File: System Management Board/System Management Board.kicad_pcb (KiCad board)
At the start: 4 copper layers, 150 x 110 mm, 55 parts, among them J1 Conn_01x04_Male, J2 Conn_01x04_Male, J3 Conn_01x02_Male, J4 PJ-063BH, J5 Conn_01x02_Male, J6 Conn_02x06_Counter_Clockwise, J7 Conn_02x20_Odd_Even, J8 Conn_01x02_Male, J9 Conn_01x02_Male, K1 J115F11CH5VDCS61.5U, K2 J114FL1CS165VDC.41, K3 J114FL1CS165VDC.41, U1 SC0915, U2 OKI-78SR-5/1.5-W36E-C, U3 OKI-78SR-5/1.5-W36E-C, U4 NEO-M9N-00B

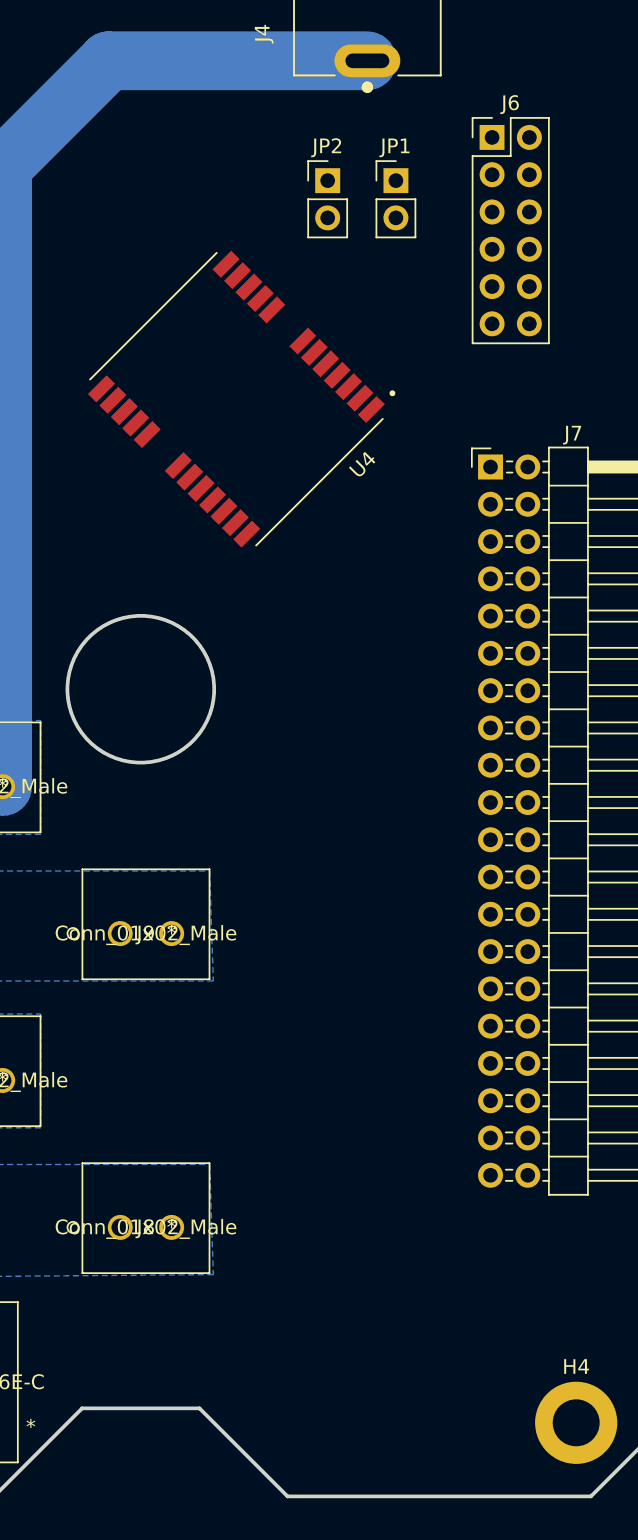
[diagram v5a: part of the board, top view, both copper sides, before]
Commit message: Removed GPS module, added GPIO connections to headder, added aux jetson header
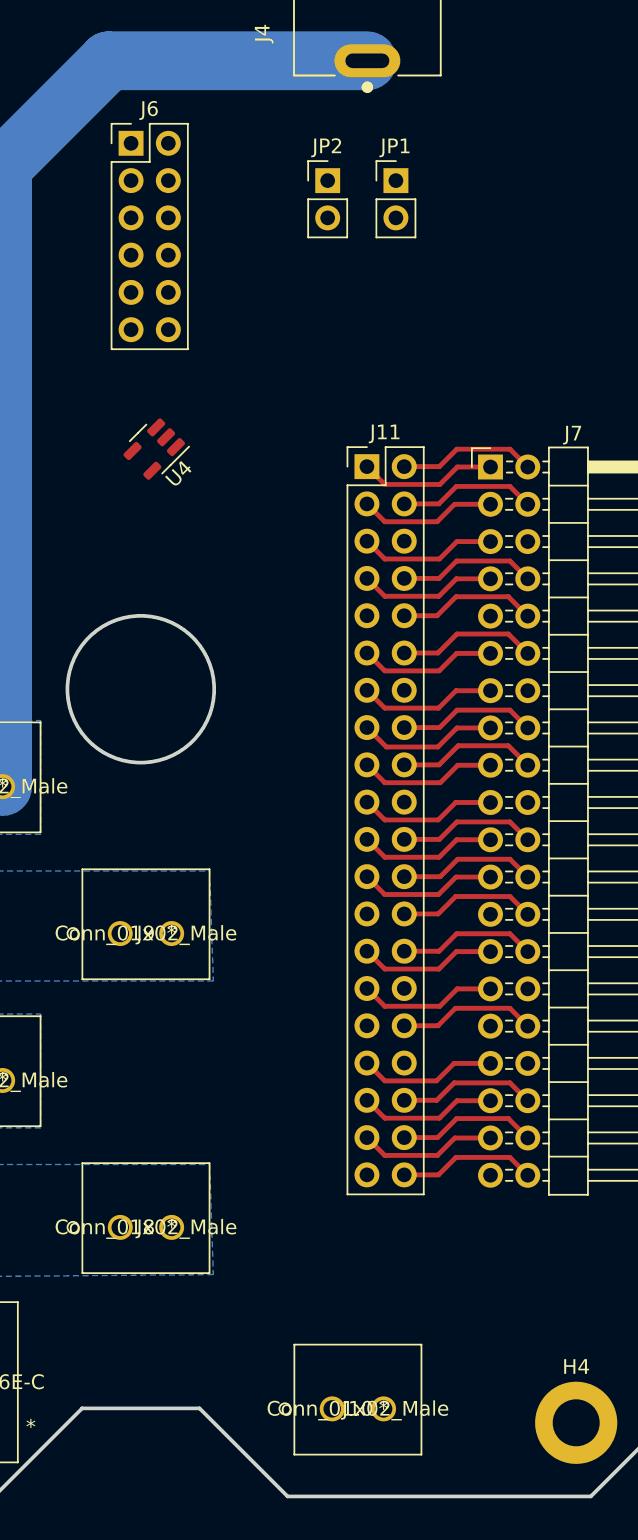
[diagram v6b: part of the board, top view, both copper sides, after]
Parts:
- added J10: Conn_01x02_Male, SMB:1843606, F.Cu at (203.6, 149.4)
- added J11: Conn_02x20_Odd_Even, Connector_PinHeader_2.54mm:PinHeader_2x20_P2.54mm_Vertical, F.Cu at (202.5, 85.2)
- U4: value NEO-M9N-00B -> AP7375-50W5-7; footprint SMB:XCVR_NEO-M9N-00B -> Package_TO_SOT_SMD:SOT-23-5
- moved J6 24.6 mm to (186.4, 63.2)
- moved U4 6.55 mm to (188.0, 84.0)
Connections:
- J7 pad 1: unconnected-(J7-Pad1) -> /JET_P1
- J7 pad 10: unconnected-(J7-Pad10) -> /Jet_UART1_Rx
- J7 pad 11: unconnected-(J7-Pad11) -> /JET_P11
- J7 pad 12: unconnected-(J7-Pad12) -> /JET_P12
- J7 pad 13: unconnected-(J7-Pad13) -> /PICO OUT BIT 1
- J7 pad 14: unconnected-(J7-Pad14) -> GND
- J7 pad 15: unconnected-(J7-Pad15) -> /PICO OUT BIT 0
- J7 pad 16: unconnected-(J7-Pad16) -> /PICO IN BIT 0
- J7 pad 17: unconnected-(J7-Pad17) -> /JET_P17
- J7 pad 18: unconnected-(J7-Pad18) -> /PICO OUT BIT 2
- J7 pad 19: unconnected-(J7-Pad19) -> /JET_P19
- J7 pad 2: unconnected-(J7-Pad2) -> /JET_P2
- J7 pad 20: unconnected-(J7-Pad20) -> GND
- J7 pad 21: unconnected-(J7-Pad21) -> /JET_P21
- J7 pad 22: unconnected-(J7-Pad22) -> /PICO IN BIT 2
- J7 pad 23: unconnected-(J7-Pad23) -> /JET_P23
- J7 pad 24: unconnected-(J7-Pad24) -> /JET_P24
- J7 pad 25: unconnected-(J7-Pad25) -> GND
- J7 pad 26: unconnected-(J7-Pad26) -> /JET_P26
- J7 pad 27: unconnected-(J7-Pad27) -> /JET_P27
- J7 pad 28: unconnected-(J7-Pad28) -> /JET_P28
- J7 pad 29: unconnected-(J7-Pad29) -> /JET_P29
- J7 pad 3: unconnected-(J7-Pad3) -> /JET_P3
- J7 pad 30: unconnected-(J7-Pad30) -> GND
- J7 pad 31: unconnected-(J7-Pad31) -> /JET_P31
- J7 pad 32: unconnected-(J7-Pad32) -> /PICO IN BIT 1
- J7 pad 33: unconnected-(J7-Pad33) -> /JET_P33
- J7 pad 34: unconnected-(J7-Pad34) -> GND
- J7 pad 35: unconnected-(J7-Pad35) -> /JET_P35
- J7 pad 36: unconnected-(J7-Pad36) -> /JET_P36
- J7 pad 37: unconnected-(J7-Pad37) -> /JET_P37
- J7 pad 38: unconnected-(J7-Pad38) -> /JET_P38
- J7 pad 39: unconnected-(J7-Pad39) -> GND
- J7 pad 4: unconnected-(J7-Pad4) -> /JET_P4
- J7 pad 40: unconnected-(J7-Pad40) -> /JET_P40
- J7 pad 5: unconnected-(J7-Pad5) -> /JET_P5
- J7 pad 6: unconnected-(J7-Pad6) -> GND
- J7 pad 7: unconnected-(J7-Pad7) -> /JET_P7
- J7 pad 8: unconnected-(J7-Pad8) -> /Jet_UART1_Tx
- J7 pad 9: unconnected-(J7-Pad9) -> GND
- U1 pad 1: unconnected-(U1-Pad1) -> /PICO IN BIT 0
- U1 pad 2: unconnected-(U1-Pad2) -> /PICO IN BIT 1
- U1 pad 31: unconnected-(U1-Pad31) -> /Vin_MES_ADC
- U1 pad 39: unconnected-(U1-Pad39) -> /5V Logic PWR
- U1 pad 4: unconnected-(U1-Pad4) -> /PICO IN BIT 2
- U1 pad 5: unconnected-(U1-Pad5) -> /PICO OUT BIT 0
- U1 pad 6: unconnected-(U1-Pad6) -> /PICO OUT BIT 1
- U1 pad 7: unconnected-(U1-Pad7) -> /PICO OUT BIT 2
- U2 pad 1: unconnected-(U2-Pad1) -> /V_batt+ PROT SW
- U2 pad 2: unconnected-(U2-Pad2) -> GND
- U2 pad 3: unconnected-(U2-Pad3) -> /5V Relay PWR
- U3 pad 1: unconnected-(U3-Pad1) -> /V_batt+ PROT SW
- U3 pad 2: unconnected-(U3-Pad2) -> GND
- U3 pad 3: unconnected-(U3-Pad3) -> /5V Logic PWR
- U4 pad 1: unconnected-(U4-Pad1) -> /V_batt+ PROT
- U4 pad 2: unconnected-(U4-Pad2) -> GND
- U4 pad 3: unconnected-(U4-Pad3) -> /Switched PWR IN PROT
- U4 pad 4: unconnected-(U4-Pad4) -> (no net)
- U4 pad 5: unconnected-(U4-Pad5) -> /5V Logic PWR
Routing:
- net /JET_P38: track 0.00 -> 9.51 mm
- net /PICO OUT BIT 2: track 0.00 -> 9.51 mm
- net /Jet_UART1_Rx: track 0.00 -> 9.51 mm
- net /PICO OUT BIT 0: track 0.00 -> 9.51 mm
- net /JET_P12: track 0.00 -> 9.50 mm
- net /PICO IN BIT 0: track 0.00 -> 9.41 mm
- net /Jet_UART1_Tx: track 0.00 -> 9.41 mm
- net /JET_P36: track 0.00 -> 9.41 mm
- net /JET_P26: track 0.00 -> 9.41 mm
- net /JET_P40: track 0.00 -> 9.41 mm
- net /JET_P2: track 0.00 -> 9.41 mm
- net /JET_P7: track 0.00 -> 9.41 mm
- net /JET_P5: track 0.00 -> 9.41 mm
- net /JET_P37: track 0.00 -> 9.41 mm
- net /JET_P35: track 0.00 -> 9.41 mm
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
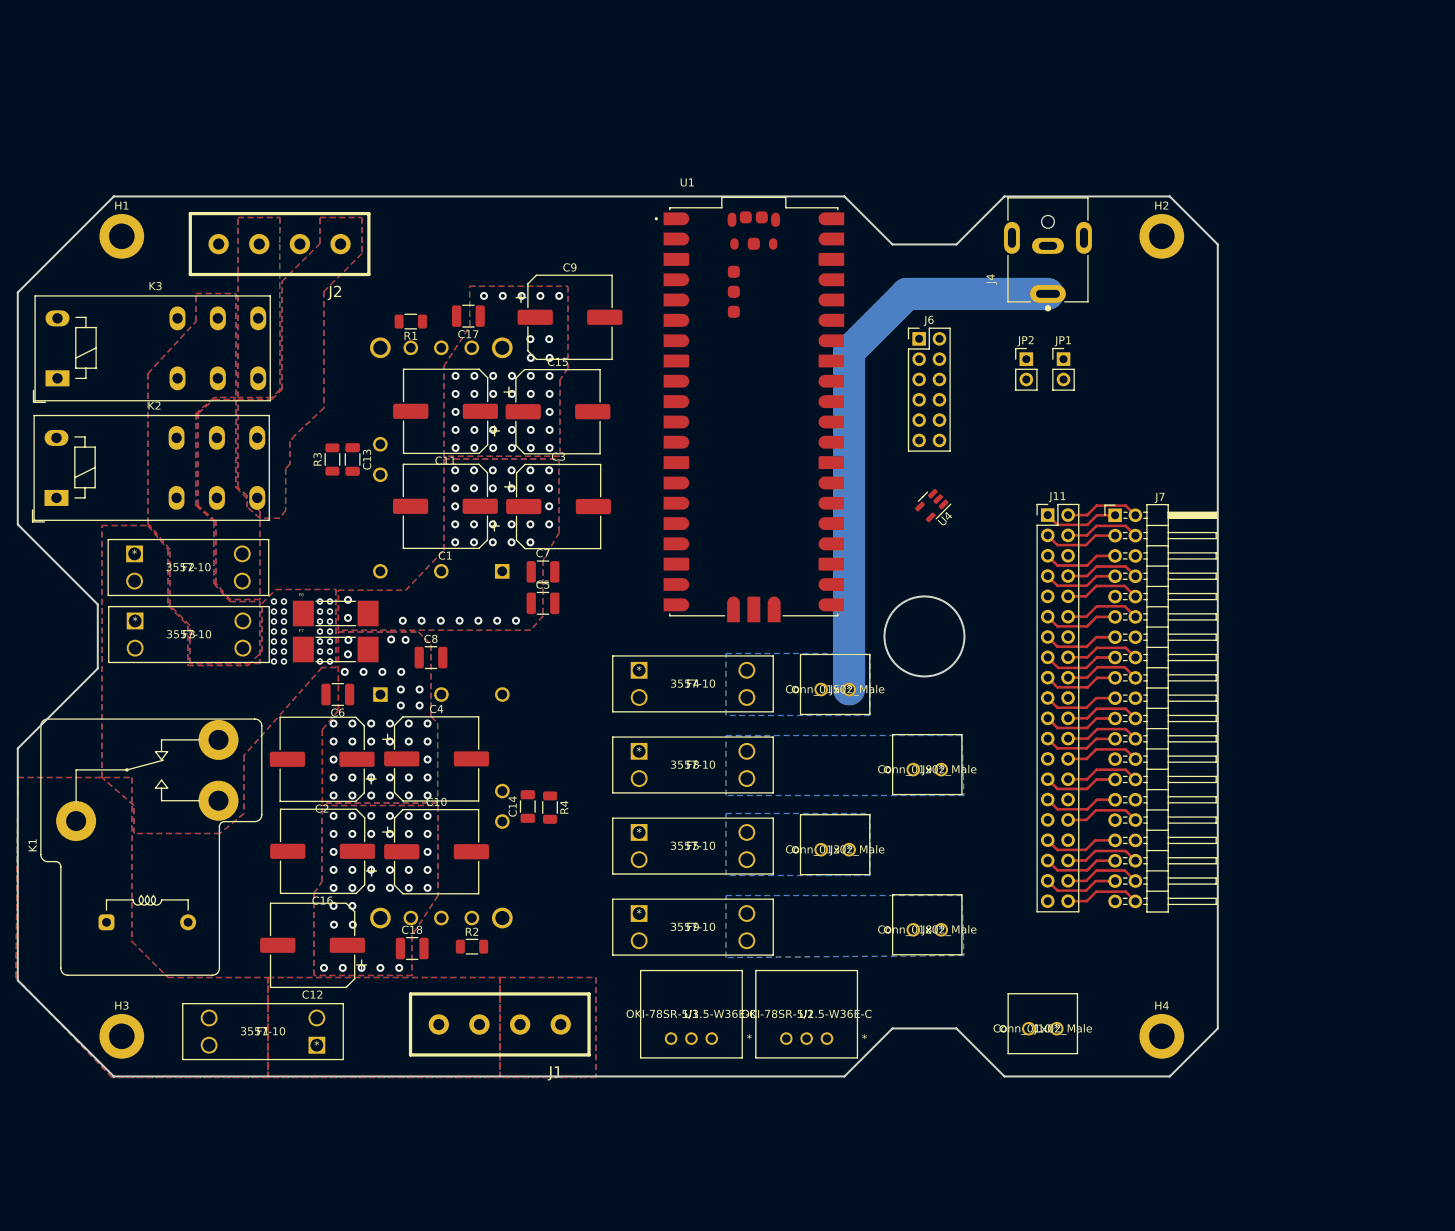
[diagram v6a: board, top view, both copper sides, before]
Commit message: Finished all high current connections
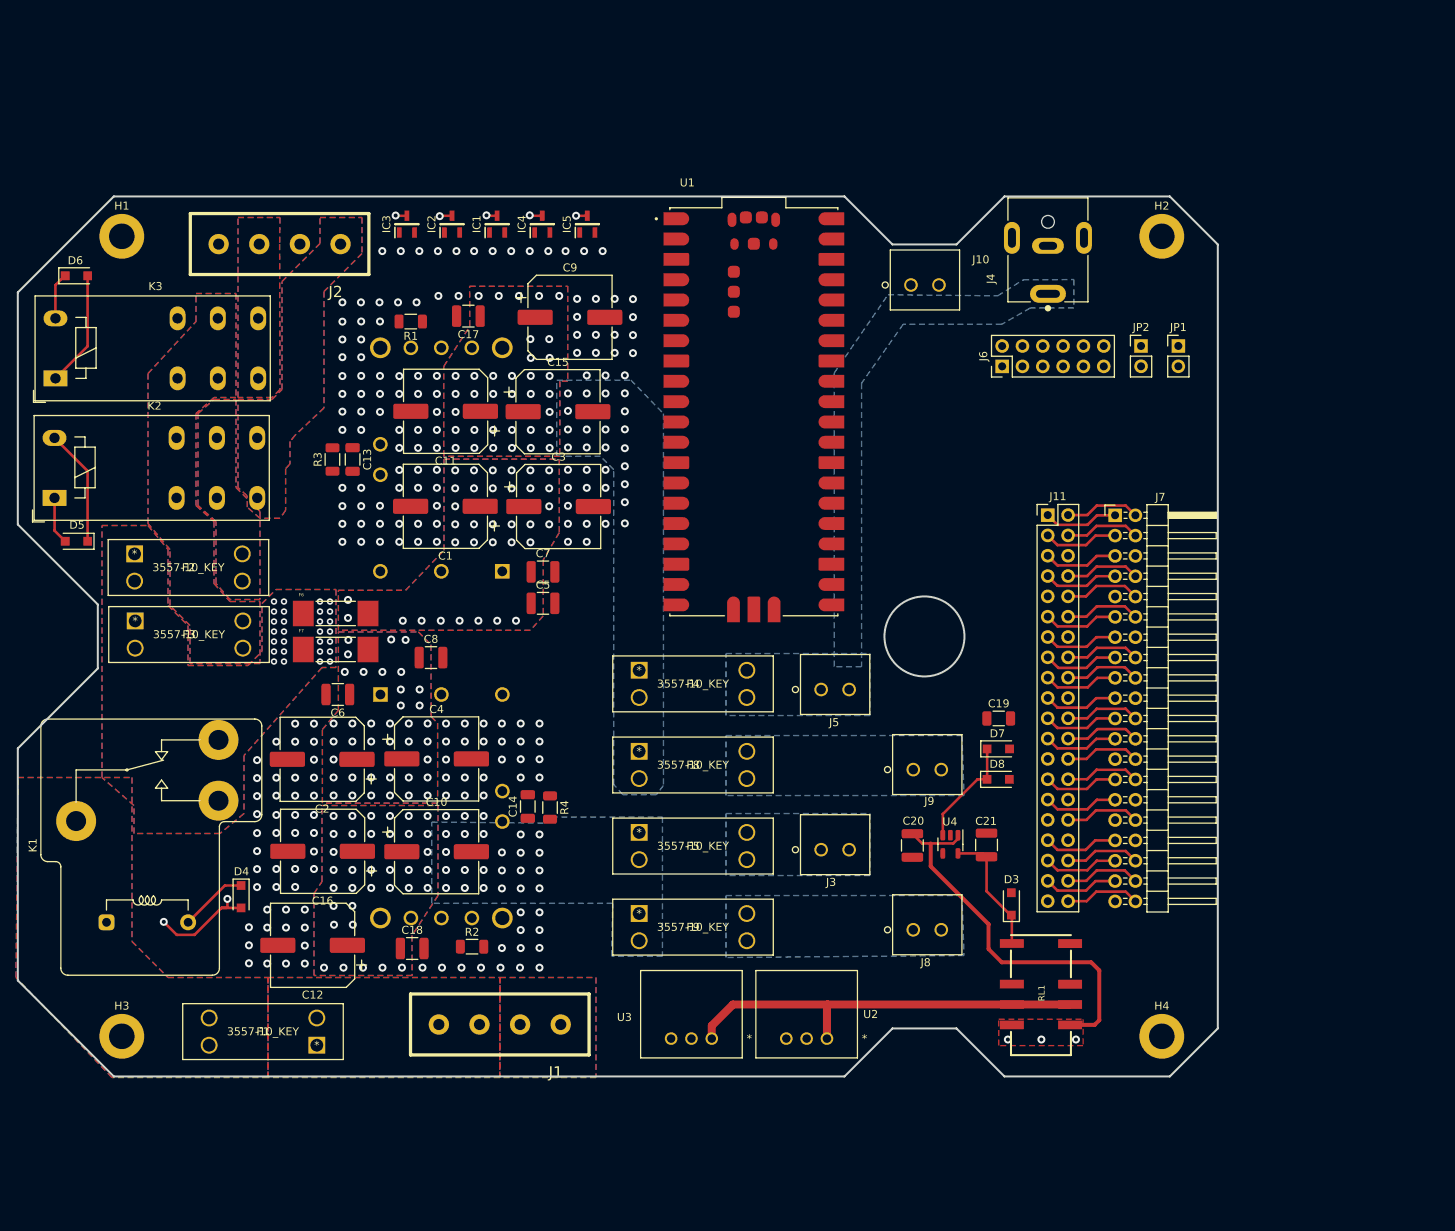
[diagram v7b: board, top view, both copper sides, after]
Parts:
- added C19: 0.1uF, Capacitor_SMD:C_1206_3216Metric, F.Cu at (196.3, 110.6)
- added C20: 10uF, Capacitor_SMD:C_1210_3225Metric, F.Cu at (185.5, 126.5)
- added C21: 10uF, Capacitor_SMD:C_1210_3225Metric, F.Cu at (194.8, 126.4)
- added D3: D, Diode_SMD:D_SOD-123F, F.Cu at (197.9, 133.8)
- added D4: D, Diode_SMD:D_SOD-123F, F.Cu at (101.6, 132.9)
- added D5: D, Diode_SMD:D_SOD-123F, F.Cu at (81.1, 88.5)
- added D6: D, Diode_SMD:D_SOD-123F, F.Cu at (81.1, 55.3)
- added D7: D, Diode_SMD:D_SOD-123F, F.Cu at (196.3, 114.4)
- added D8: D, Diode_SMD:D_SOD-123F, F.Cu at (196.3, 118.2)
- added IC1: SI2318CDS-T1-GE3, SMB:SOT95P237X112-3N, F.Cu at (133.6, 48.8)
- added IC2: SI2318CDS-T1-GE3, SMB:SOT95P237X112-3N, F.Cu at (128.0, 48.8)
- added IC3: SI2318CDS-T1-GE3, SMB:SOT95P237X112-3N, F.Cu at (122.4, 48.8)
- added IC4: SI2318CDS-T1-GE3, SMB:SOT95P237X112-3N, F.Cu at (139.3, 48.8)
- added IC5: SI2318CDS-T1-GE3, SMB:SOT95P237X112-3N, F.Cu at (144.9, 48.8)
- added RL1: EE2-5NU, SMB:EE2-5NU, F.Cu at (201.7, 144.9)
- F1, F2, F3, F4, F5, F8, F9: value 3557-10 -> 3557-10_KEY
- K2, K3: footprint SMB:Relay_SPDT_Schrack-RT1-16A-FormC_RM5mm -> Relay_THT:Relay_SPDT_Schrack-RT1-16A-FormC_RM5mm
- moved J10 94.1 mm to (188.9, 56.4)
- moved U4 42.4 mm to (190.3, 126.3), turned to -90 degrees
- moved JP1 14.4 mm to (218.8, 64.1)
- moved JP2 14.4 mm to (214.1, 64.1)
- moved J6 10.9 mm to (196.8, 66.6), turned to 90 degrees
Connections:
- J10 pad 2: /Switched PWR IN PROT -> Net-(J10-Pad2)
- K1 pad A1: unconnected-(K1-PadA1) -> Net-(K1-PadA1)
- K1 pad A2: unconnected-(K1-PadA2) -> /5V Relay PWR
- K2 pad A1: unconnected-(K2-PadA1) -> Net-(K2-PadA1)
- K2 pad A2: unconnected-(K2-PadA2) -> /5V Relay PWR
- K3 pad A1: unconnected-(K3-PadA1) -> Net-(K3-PadA1)
- K3 pad A2: unconnected-(K3-PadA2) -> /5V Relay PWR
- U1 pad 10: unconnected-(U1-Pad10) -> /Light A Relay EN
- U1 pad 13: Net-(U1-Pad13) -> GND
- U1 pad 14: unconnected-(U1-Pad14) -> /Light B Relay EN
- U1 pad 15: unconnected-(U1-Pad15) -> /COMP PWR EN
- U1 pad 16: unconnected-(U1-Pad16) -> /SWITCH PWR EN
- U1 pad 18: Net-(U1-Pad13) -> GND
- U1 pad 23: Net-(U1-Pad13) -> GND
- U1 pad 28: Net-(U1-Pad13) -> GND
- U1 pad 3: Net-(U1-Pad13) -> GND
- U1 pad 30: unconnected-(U1-Pad30) -> Net-(U1-Pad30)
- U1 pad 33: unconnected-(U1-Pad33) -> GND
- U1 pad 38: Net-(U1-Pad13) -> GND
- U1 pad 8: Net-(U1-Pad13) -> GND
- U1 pad 9: unconnected-(U1-Pad9) -> /Main Relay EN
- U1 pad A: Net-(U1-PadA) -> unconnected-(U1-PadA)
- U1 pad B: Net-(U1-PadA) -> unconnected-(U1-PadA)
- U1 pad C: Net-(U1-PadA) -> unconnected-(U1-PadA)
- U1 pad D: Net-(U1-PadA) -> unconnected-(U1-PadA)
- U1 pad D2: Net-(U1-Pad13) -> GND
- U2 pad 1: /V_batt+ PROT SW -> Net-(RL1-PadC1)
- U3 pad 1: /V_batt+ PROT SW -> Net-(RL1-PadC1)
- U4 pad 5: /5V Logic PWR -> Net-(D3-Pad1)
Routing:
- net /5V Relay PWR: track 0.00 -> 209.3 mm
- net /V_batt+ PROT: track 0.00 -> 155.0 mm, vias 0 -> 3
- net Net-(K1-PadA1): track 0.00 -> 137.4 mm, vias 0 -> 3
- net Net-(K2-PadA1): track 0.00 -> 80.0 mm, vias 0 -> 1
- net /~{SWITCH PWR EN}: track 0.00 -> 76.7 mm, vias 0 -> 1
- net /COMP PWR OUT PROT: track 70.1 -> 0.00 mm
- net Net-(K3-PadA1): track 0.00 -> 68.5 mm, vias 0 -> 1
- net /~{COMP PWR EN}: track 0.00 -> 55.4 mm, vias 0 -> 1
- net Net-(RL1-PadC1): track 0.00 -> 51.8 mm
- net Net-(D3-Pad1): track 0.00 -> 15.9 mm
- net /Switched PWR IN PROT: track 0.00 -> 13.8 mm
- net GND: vias 0 -> 229
